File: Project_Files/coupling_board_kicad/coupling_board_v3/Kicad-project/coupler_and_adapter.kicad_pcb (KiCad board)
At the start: 2 copper layers, 98.8 x 70 mm, 95 parts, among them IC1 ISO6741DWR, IC2 ISO6740FDWR, IC3 ISO6740FDWR, J1 Conn_02x04_Odd_Even, J1 Molex Microfit, J10 Conn_02x12_Odd_Even, J2 Conn_02x04_Odd_Even, J2 Conn_02x12_Odd_Even, J3 Conn_02x04_Odd_Even, J3 Molex6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

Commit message: Updated design files
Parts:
- moved C7 36.6 mm to (108.4, 73.0)
- moved C9 36.6 mm to (115.2, 73.0)
- moved J3 36.6 mm to (106.5, 77.3)
- moved J5 36.6 mm to (153.7, 91.4)
- moved J7 36.6 mm to (114.5, 91.6)
- moved KiKit_MB_1_2 36.6 mm to (164.8, 69.4)
- moved KiKit_MB_2_2 36.6 mm to (164.8, 81.0)
- moved KiKit_MB_2_3 36.6 mm to (164.8, 80.2)
- moved KiKit_MB_3_3 36.6 mm to (164.8, 91.9)
- moved KiKit_MB_6_5 36.6 mm to (162.0, 69.4)
- moved KiKit_MB_7_4 36.6 mm to (162.0, 80.2)
- moved KiKit_MB_7_5 36.6 mm to (162.0, 81.0)
- moved KiKit_MB_8_4 36.6 mm to (162.0, 91.9)
- moved C1 36.6 mm to (145.5, 101.2)
- moved C3 36.6 mm to (145.6, 77.1)
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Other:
- outline, holes or cut-outs redrawn

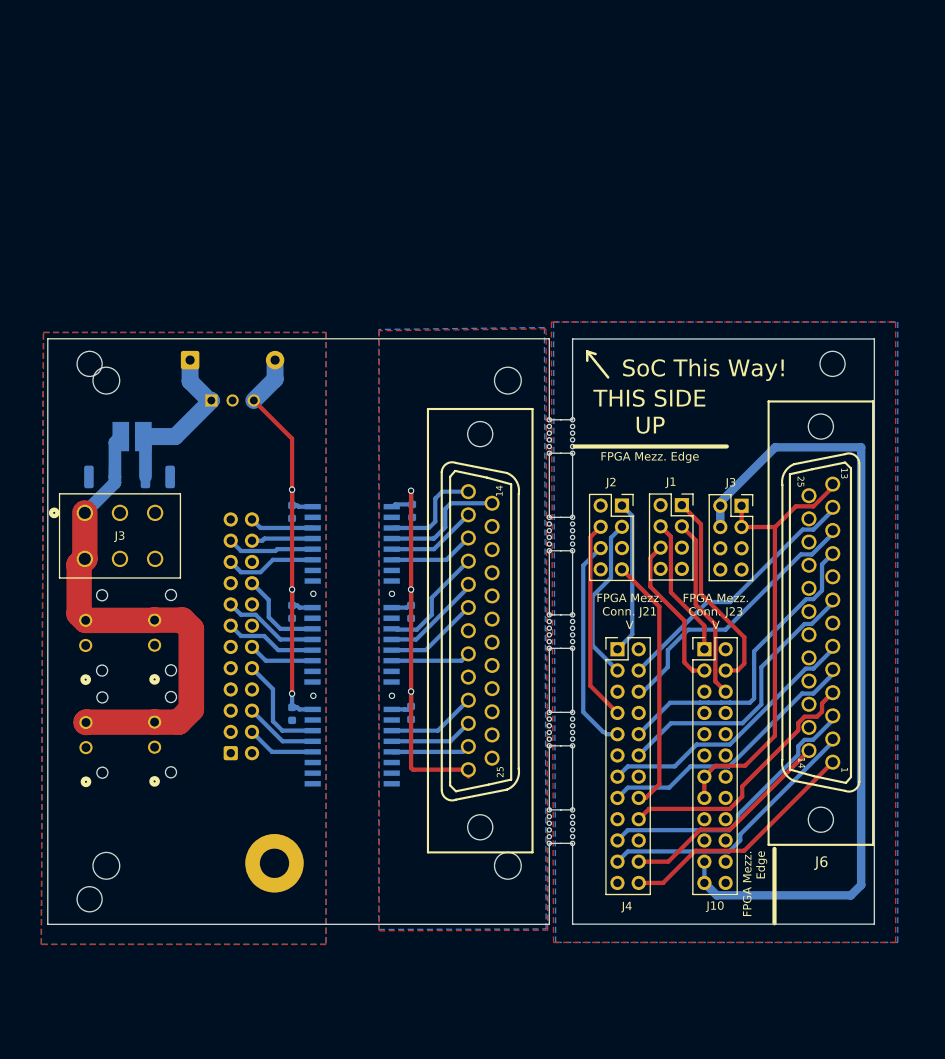
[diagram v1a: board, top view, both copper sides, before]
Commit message: Updated design, added digikey bom
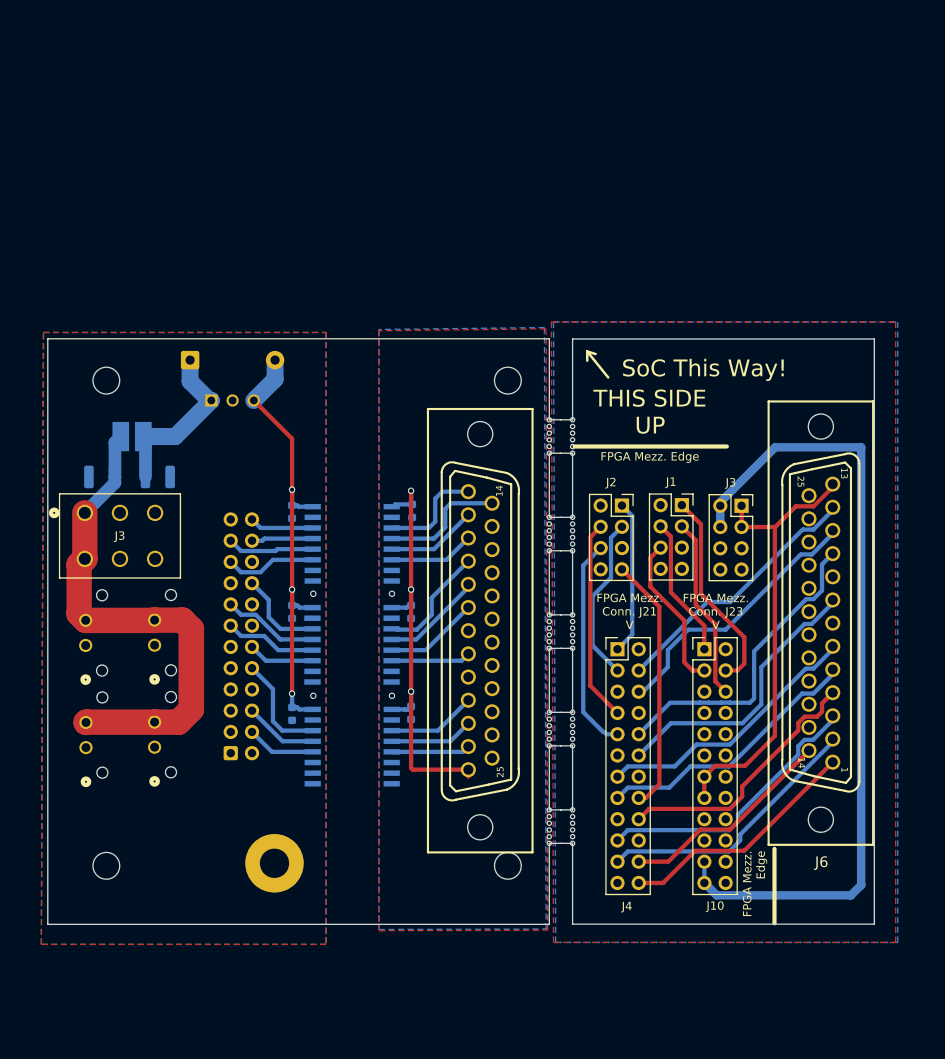
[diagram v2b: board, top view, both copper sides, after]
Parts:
- removed KiKit_TO_1, KiKit_TO_2, KiKit_TO_3: NPTH, NPTH
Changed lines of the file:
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@@
-	(footprint "NPTH"
-		(layer "F.Cu")
-		(at 107.04 123.491)
-		(property "Reference" "KiKit_TO_3"
-			(at 0 0.5 0)
-			(layer "F.SilkS")
-			(hide yes)
-			(effects
-				(font
-					(size 1 1)
-					(thickness 0.15)
-				)
-			)
-		)
-		(property "Value" "NPTH"
-			(at 0 -0.5 0)
-			(layer "F.Fab")
-			(hide yes)
-			(effects
-				(font
-					(size 1 1)
-					(thickness 0.15)
-				)
-			)
-		)
-		(property "Datasheet" ""
-			(at 0 0 0)
-			(layer "F.Fab")
-			(hide yes)
-			(effects
-				(font
-					(size 1.27 1.27)
-					(thickness 0.15)
-				)
-			)
-		)
-		(property "Description" ""
-			(at 0 0 0)
-			(layer "F.Fab")
-			(hide yes)
-			(effects
-				(font
-					(size 1.27 1.27)
-					(thickness 0.15)
-				)
-			)
-		)
-		(solder_mask_margin 0)
-		(attr through_hole board_only exclude_from_bom)
-		(pad "" np_thru_hole circle
-			(at 0 0)
-			(size 3 3)
-			(drill 3)
-			(layers "*.Mask")
-		)
-		(embedded_fonts no)
-	)
 	(footprint "NPTH"
 		(layer "F.Cu")
@@
 			(size 0.5 0.5)
 			(drill 0.5)
-			(layers "*.Mask")
-		)
-		(embedded_fonts no)
-	)
-	(footprint "NPTH"
-		(layer "F.Cu")
-		(at 195.85 59.491)
-		(property "Reference" "KiKit_TO_2"
-			(at 0 0.5 0)
-			(layer "F.SilkS")
-			(hide yes)
-			(effects
-				(font
-					(size 1 1)
-					(thickness 0.15)
-				)
-			)
-		)
-		(property "Value" "NPTH"
-			(at 0 -0.5 0)
-			(layer "F.Fab")
-			(hide yes)
-			(effects
-				(font
-					(size 1 1)
-					(thickness 0.15)
-				)
-			)
-		)
-		(property "Datasheet" ""
-			(at 0 0 0)
-			(layer "F.Fab")
-			(hide yes)
-			(effects
-				(font
-					(size 1.27 1.27)
-					(thickness 0.15)
-				)
-			)
-		)
-		(property "Description" ""
-			(at 0 0 0)
-			(layer "F.Fab")
-			(hide yes)
-			(effects
-				(font
-					(size 1.27 1.27)
-					(thickness 0.15)
-				)
-			)
-		)
-		(solder_mask_margin 0)
-		(attr through_hole board_only exclude_from_bom)
-		(pad "" np_thru_hole circle
-			(at 0 0)
-			(size 3 3)
-			(drill 3)
 			(layers "*.Mask")
 		)
@@
 			(layers "*.Mask")
 		)
-		(embedded_fonts no)
-	)
-	(footprint "NPTH"
-		(layer "F.Cu")
-		(at 107.04 59.491)
-		(property "Reference" "KiKit_TO_1"
-			(at 0 0.5 0)
-			(layer "F.SilkS")
-			(hide yes)
-			(effects
-				(font
-					(size 1 1)
-					(thickness 0.15)
-				)
-			)
-		)
-		(property "Value" "NPTH"
-			(at 0 -0.5 0)
-			(layer "F.Fab")
-			(hide yes)
-			(effects
-				(font
-					(size 1 1)
-					(thickness 0.15)
-				)
-			)
-		)
-		(property "Datasheet" ""
-			(at 0 0 0)
-			(layer "F.Fab")
-			(hide yes)
-			(effects
-				(font
-					(size 1.27 1.27)
-					(thickness 0.15)
-				)
-			)
-		)
-		(property "Description" ""
-			(at 0 0 0)
-			(layer "F.Fab")
-			(hide yes)
-			(effects
-				(font
-					(size 1.27 1.27)
-					(thickness 0.15)
-				)
-			)
-		)
-		(solder_mask_margin 0)
-		(attr through_hole board_only exclude_from_bom)
-		(pad "" np_thru_hole circle
-			(at 0 0)
-			(size 3 3)
-			(drill 3)
-			(layers "*.Mask")
-		)

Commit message: Updated design
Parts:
- removed the J1 at (177.8, 76.4)
- removed the J1 at (106.3, 91.7)
- removed the J2 at (170.7, 76.4)
- removed the J2 at (123.9, 106.0)
- removed the J3 at (106.5, 77.3)
- removed the J3 at (185.0, 76.5)
- added J1: Conn_02x04_Odd_Even, Connector_PinSocket_2.54mm:PinSocket_2x04_P2.54mm_Vertical, F.Cu at (181.4, 88.0)
- added J1: Molex Microfit, ul_436500215:CONN_SD-43650-006_02_MOL, B.Cu at (109.9, 103.3)
- added J2: Conn_02x04_Odd_Even, Connector_PinSocket_2.54mm:PinSocket_2x04_P2.54mm_Vertical, F.Cu at (174.3, 88.1)
- added J2: Conn_02x12_Odd_Even, Connector_IDC:IDC-Header_2x12_P2.54mm_Vertical, B.Cu at (127.5, 117.7)
- added J3: Conn_02x04_Odd_Even, Connector_PinSocket_2.54mm:PinSocket_2x04_P2.54mm_Vertical, F.Cu at (188.6, 88.1)
- added J3: Molex6, ul_0039281063-5566-06A:CONN_0039281063_5566-06A_MOL, F.Cu at (110.1, 89.0)
- moved H3 12.2 mm to (160.6, 131.1)
- moved H2 12.2 mm to (112.6, 131.1)
- moved KiKit_MB_10_6 12.2 mm to (165.6, 128.5)
- moved KiKit_MB_5_1 12.2 mm to (168.4, 128.5)
- moved C1 12.2 mm to (149.1, 112.9)
- moved C2 12.2 mm to (149.1, 100.8)
- moved H4 12.2 mm to (160.6, 73.1)
- moved H5 12.2 mm to (132.7, 130.8)
- moved J6 12.2 mm to (198.1, 102.1)
- moved D1 12.2 mm to (122.7, 70.7)
- moved C9 12.2 mm to (118.8, 84.7)
- moved J9 12.2 mm to (109.9, 115.5)
- moved PS1 12.2 mm to (125.2, 75.5)
- moved C3 12.2 mm to (149.2, 88.7)
- moved C4 12.2 mm to (134.8, 88.8)
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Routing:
- net Board_0-GND1: track 0.00 -> 11.0 mm, vias 0 -> 4
- net Board_0-3V3_VCUT: track 97.3 -> 98.4 mm
- net Board_1-Vin: track 60.3 -> 60.8 mm
- net Board_1-GND1: vias 2 -> 7

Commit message: Committing prototyped DRC checked version
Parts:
- removed the J1 at (181.4, 88.0)
- removed the J1 at (109.9, 103.3)
- removed the J2 at (174.3, 88.1)
- removed the J2 at (127.5, 117.7)
- removed the J3 at (188.6, 88.1)
- removed the J3 at (110.1, 89.0)
- added J1: Conn_02x04_Odd_Even, Connector_PinSocket_2.54mm:PinSocket_2x04_P2.54mm_Vertical, F.Cu at (174.9, 39.9)
- added J1: Molex Microfit, ul_436500215:CONN_SD-43650-006_02_MOL, B.Cu at (103.3, 55.2)
- added J2: Conn_02x04_Odd_Even, Connector_PinSocket_2.54mm:PinSocket_2x04_P2.54mm_Vertical, F.Cu at (167.7, 39.9)
- added J2: Conn_02x12_Odd_Even, Connector_IDC:IDC-Header_2x12_P2.54mm_Vertical, B.Cu at (121.0, 69.5)
- added J3: Conn_02x04_Odd_Even, Connector_PinSocket_2.54mm:PinSocket_2x04_P2.54mm_Vertical, F.Cu at (182.0, 40.0)
- added J3: Molex6, ul_0039281063-5566-06A:CONN_0039281063_5566-06A_MOL, F.Cu at (103.5, 40.8)
- moved H2 48.6 mm to (106.1, 83.0)
- moved H3 48.6 mm to (154.1, 83.0)
- moved KiKit_MB_10_6 48.6 mm to (159.0, 80.3)
- moved KiKit_MB_5_1 48.6 mm to (161.8, 80.3)
- moved C7 48.6 mm to (105.5, 36.5)
- moved C9 48.6 mm to (112.2, 36.5)
- moved D1 48.6 mm to (116.1, 22.5)
- moved J5 48.6 mm to (150.8, 54.9)
- moved J7 48.6 mm to (111.5, 55.1)
- moved KiKit_MB_1_2 48.6 mm to (161.8, 32.9)
- moved KiKit_MB_2_2 48.6 mm to (161.8, 44.5)
- moved KiKit_MB_2_3 48.6 mm to (161.8, 43.7)
- moved KiKit_MB_3_3 48.6 mm to (161.8, 55.4)
- moved KiKit_MB_6_5 48.6 mm to (159.0, 32.9)
- moved KiKit_MB_7_4 48.6 mm to (159.0, 43.7)
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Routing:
- net Board_1-GND1: track 0.00 -> 38.3 mm
- net Board_0-GND1: track 11.0 -> 25.0 mm
- net Board_1-VDD: track 53.7 -> 52.9 mm
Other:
- outline, holes or cut-outs redrawn
